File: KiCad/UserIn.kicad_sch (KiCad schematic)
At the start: 4 parts, among them SW2 SW_Push, SW3 SW_Push, SW4 SW_Push, SW7 SW_Push

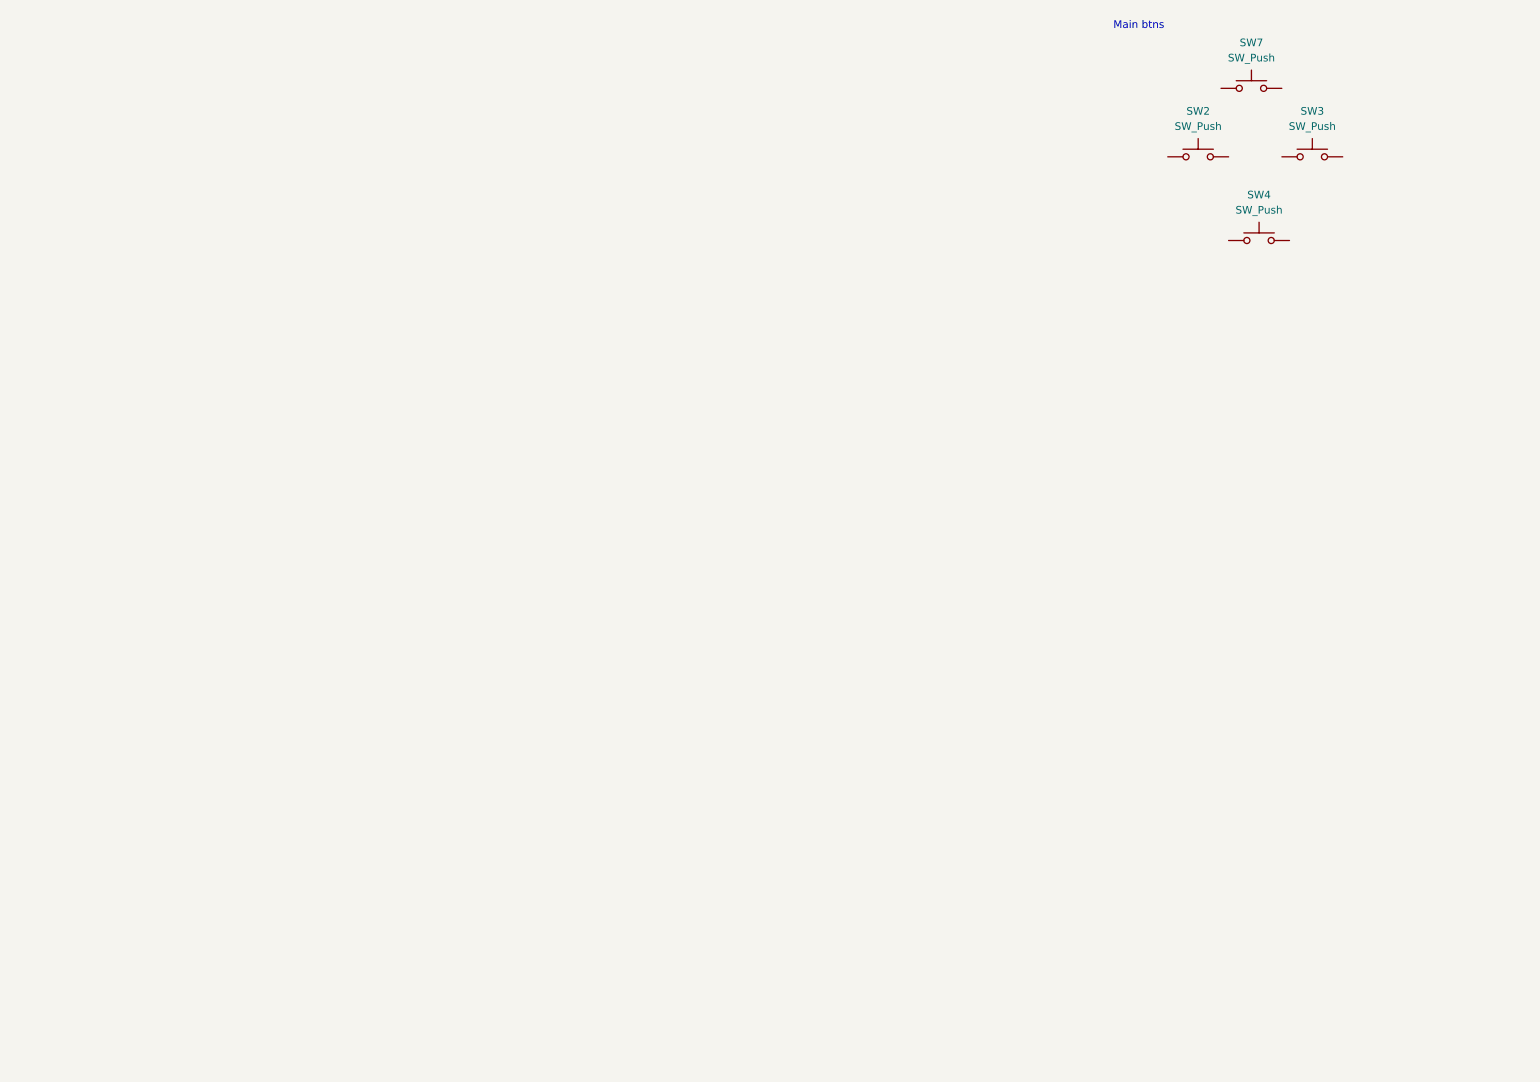
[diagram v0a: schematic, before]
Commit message: added hierachical sheets to controllers
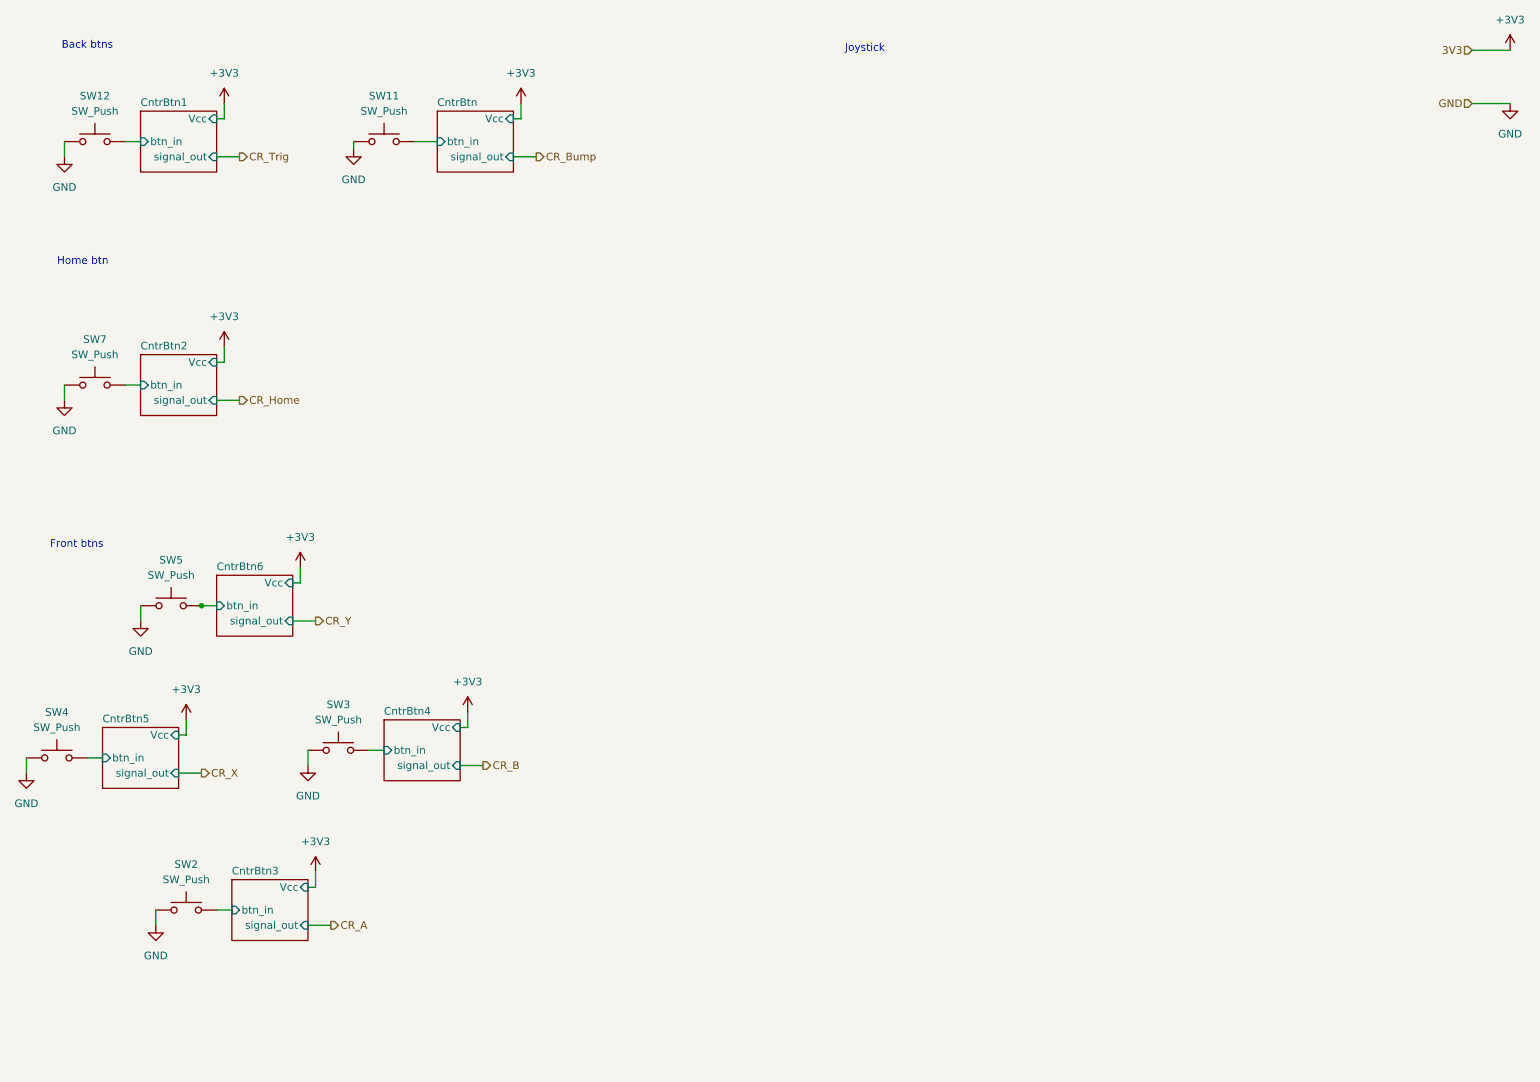
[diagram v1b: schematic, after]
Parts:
- added SW11, SW12, SW5: SW_Push, symbol CM5_HighSpeedBreakout:SW_Push
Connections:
- net GND: now reaches SW2.1
- net GND: now also SW3.1, SW4.1, SW7.1, SW11.1, SW12.1, SW5.1
- net CntrBtn3/btn_in: now reaches SW2.2
- net CntrBtn5/btn_in: now reaches SW4.2
- net CntrBtn2/btn_in: now reaches SW7.2
- net CntrBtn4/btn_in: now reaches SW3.2
- new net CntrBtn/btn_in: SW11.2
- new net CntrBtn1/btn_in: SW12.2
- new net CntrBtn6/btn_in: SW5.2
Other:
- added sheet CntrBtn (CntrBtn.kicad_sch)
- added sheet CntrBtn1 (CntrBtn.kicad_sch)
- added sheet CntrBtn2 (CntrBtn.kicad_sch)
- added sheet CntrBtn3 (CntrBtn.kicad_sch)
- added sheet CntrBtn4 (CntrBtn.kicad_sch)
- added sheet CntrBtn5 (CntrBtn.kicad_sch)
- added sheet CntrBtn6 (CntrBtn.kicad_sch)
- note added: "Back btns"
- note added: "Front btns"
- note added: "Home btn"
- note added: "Joystick"
- note removed: "Main btns"
- moved on the sheet: SW2, SW3, SW4, SW7

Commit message: redid button pull up. Added initial joystick and display symbols
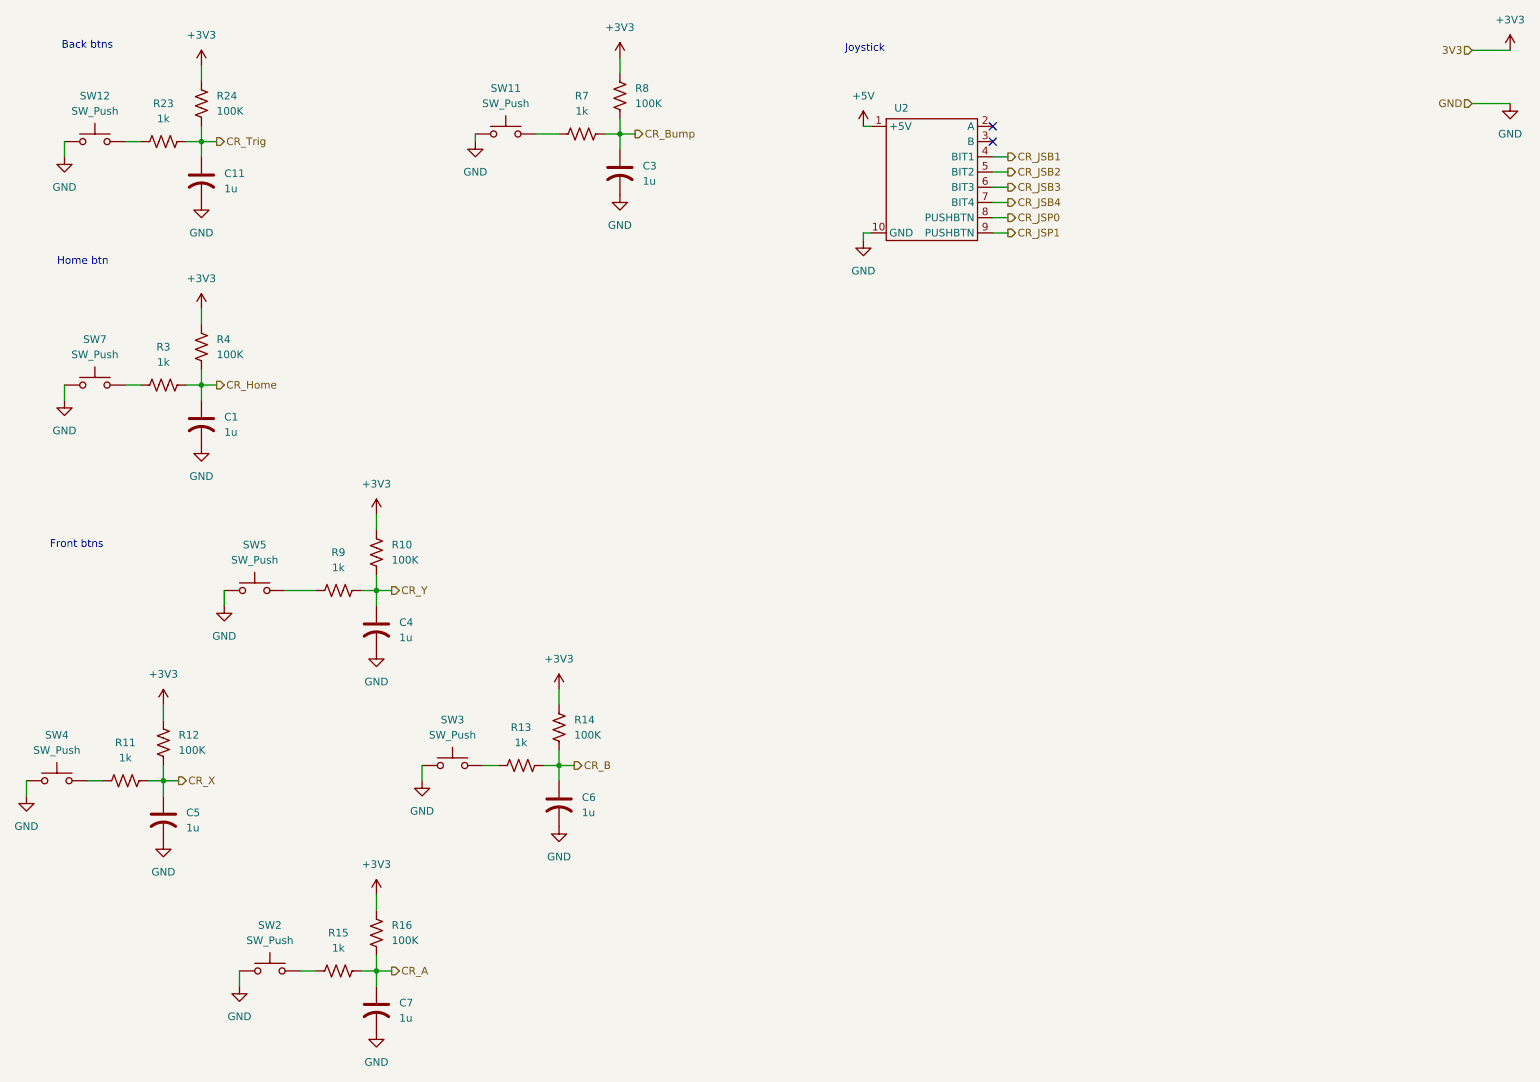
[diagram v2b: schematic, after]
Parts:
- added C1, C11, C3, C4, C5, C6, C7: 1u, symbol Device:C_US
- added R10, R12, R14, R16, R24, R4, R8: 100K, symbol Device:R_US
- added R11, R13, R15, R23, R3, R7, R9: 1k, symbol Device:R_US
- added U2: ~, symbol SBC_handheld:joystick_3axis
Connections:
- net +3V3: now also R10.1, R12.1, R14.1, R16.1, R24.1, R4.1, R8.1
- net CR_A: now also C7.1, R15.2, R16.2
- net CR_B: now also C6.1, R13.2, R14.2
- net CR_Bump: now also C3.1, R7.2, R8.2
- net CR_Home: now also C1.1, R3.2, R4.2
- net CR_Trig: now also C11.1, R23.2, R24.2
- net CR_X: now also C5.1, R11.2, R12.2
- net CR_Y: now also C4.1, R10.2, R9.2
- net GND: now also C1.2, C11.2, C3.2, C4.2, C5.2, C6.2, C7.2, U2.10 (GND)
- net CntrBtn/btn_in: no longer names the net of SW11.2
- net CntrBtn/btn_in: now also R7.1
- net CntrBtn1/btn_in: no longer names the net of SW12.2
- net CntrBtn1/btn_in: now also R23.1
- net CntrBtn2/btn_in: no longer names the net of SW7.2
- net CntrBtn2/btn_in: now also R3.1
- net CntrBtn3/btn_in: no longer names the net of SW2.2
- net CntrBtn3/btn_in: now also R15.1
- net CntrBtn4/btn_in: no longer names the net of SW3.2
- net CntrBtn4/btn_in: now also R13.1
- net CntrBtn5/btn_in: no longer names the net of SW4.2
- net CntrBtn5/btn_in: now also R11.1
- net CntrBtn6/btn_in: no longer names the net of SW5.2
- net CntrBtn6/btn_in: now also R9.1
- new net +5V: U2.1 (+5V)
- new net CR_JSB1: U2.4 (BIT1)
- new net CR_JSB2: U2.5 (BIT2)
- new net CR_JSB3: U2.6 (BIT3)
- new net CR_JSB4: U2.7 (BIT4)
- new net CR_JSP0: U2.8 (PUSHBTN)
- new net CR_JSP1: U2.9 (PUSHBTN)
- no-connect marks 0 -> 2
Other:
- removed sheet CntrBtn
- removed sheet CntrBtn1
- removed sheet CntrBtn2
- removed sheet CntrBtn3
- removed sheet CntrBtn4
- removed sheet CntrBtn5
- removed sheet CntrBtn6
- moved on the sheet: SW11, SW2, SW3, SW4, SW5
